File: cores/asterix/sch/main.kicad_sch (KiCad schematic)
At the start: 39 parts

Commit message: sound and pcm done! wip objects
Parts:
- added C14: 74LS138, symbol jt74:74LS138
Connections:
- net ~{RESET} renamed ~{SYSRES}
- new net ~{MCS}: C14.13 (O2)
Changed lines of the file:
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@@
+    (stroke (width 0) (type default))
+  )
+  (wire (pts (xy 118.11 250.19) (xy 125.73 250.19))
     (stroke (width 0) (type default))
   )
@@
     (effects (font (size 1.27 1.27)) (justify left))
   )
+  (hierarchical_label "~{MCS}" (shape output) (at 125.73 250.19 0) (fields_autoplaced)
+    (effects (font (size 1.27 1.27)) (justify left))
+  )
   (hierarchical_label "MAIN~{IRQ}" (shape input) (at 50.8 52.07 180) (fields_autoplaced)
     (effects (font (size 1.27 1.27)) (justify right))
@@
     (effects (font (size 1.27 1.27)) (justify left))
   )
-  (hierarchical_label "~{RESET}" (shape input) (at 48.26 80.01 180) (fields_autoplaced)
+  (hierarchical_label "~{SYSRES}" (shape input) (at 48.26 80.01 180) (fields_autoplaced)
     (effects (font (size 1.27 1.27)) (justify right))
   )
@@
         )
       )
+    )
+  )
+  (symbol (lib_id "jt74:74LS138") (at 105.41 252.73 0) (unit 1)
+    (in_bom yes) (on_board yes) (dnp no)
+    (property "Reference" "C14" (at 111.76 241.3 0)
+      (effects (font (size 1.27 1.27)))
+    )
+    (property "Value" "74LS138" (at 109.22 266.7 0)
+      (effects (font (size 1.27 1.27)))
+    )
+    (property "Footprint" "" (at 105.41 252.73 0)
+      (effects (font (size 1.27 1.27)) hide)
+    )
+    (property "Datasheet" "http://www.ti.com/lit/gpn/sn74LS138" (at 105.41 252.73 0)
+      (effects (font (size 1.27 1.27)) hide)
+    )
+    (pin "1")
+    (pin "10")
+    (pin "11")
+    (pin "12")
+    (pin "13")
+    (pin "14")
+    (pin "15")
+    (pin "2")
+    (pin "3")
+    (pin "4")
+    (pin "5")
+    (pin "6")
+    (pin "7")
+    (pin "9")
+    (instances
+      (project "asterix"
+        (path "/0011ec10-82c4-4039-b424-337480f568e8/7d4ab3ba-37fa-4111-bbdb-c99f1a708a52"
+          (reference "C14") (unit 1)
+        )
+      )

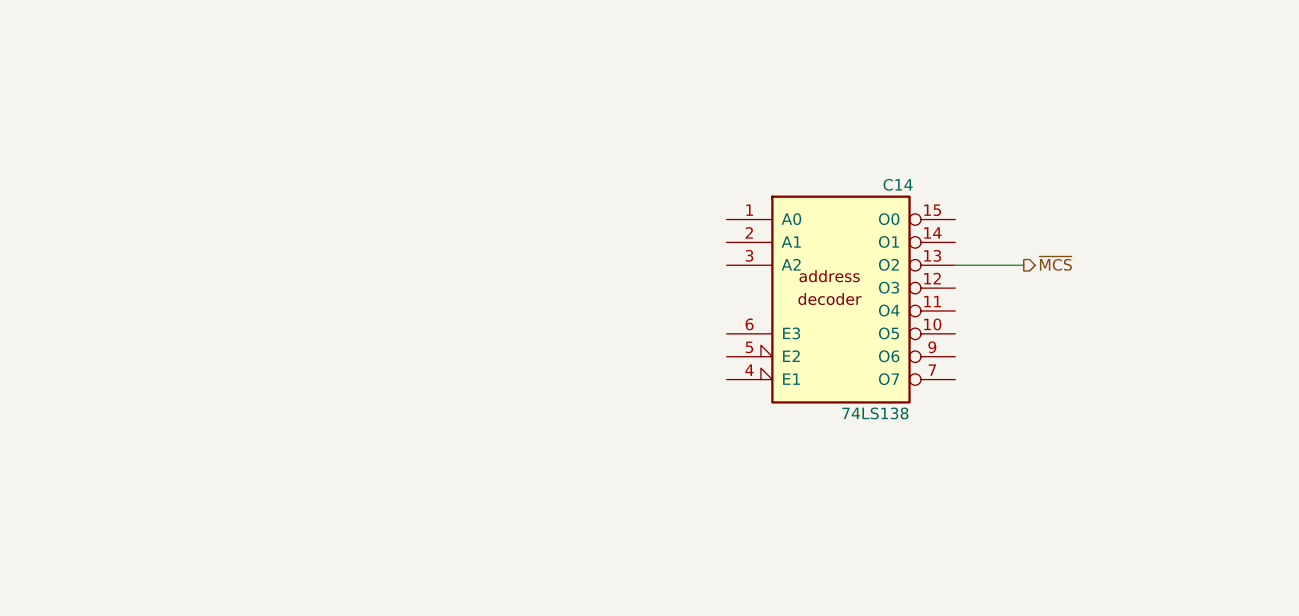
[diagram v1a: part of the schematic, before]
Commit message: objects done. wip of main, sch asterix
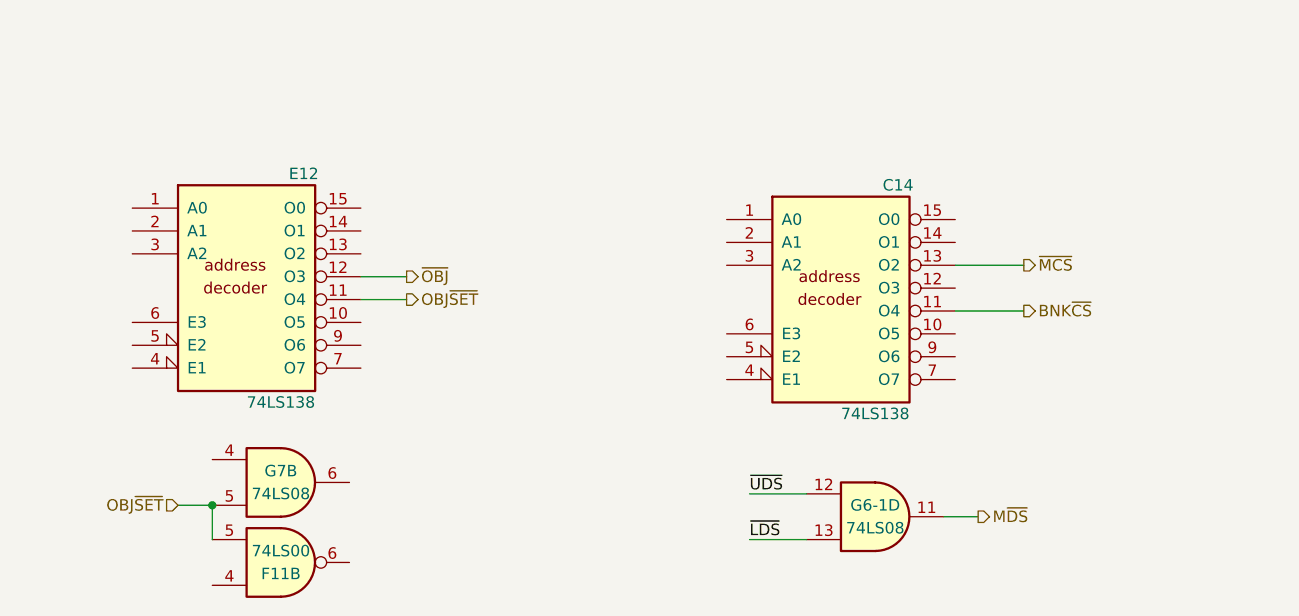
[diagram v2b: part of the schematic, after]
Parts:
- added E12: 74LS138, symbol jt74:74LS138
- added F11: 74LS00, symbol jt74:74LS00
- added G6-1, G7: 74LS08, symbol jt74:74LS08
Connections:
- net ~{LDS}: now also G6-1.13
- net ~{UDS}: now also G6-1.12
- net BNK~{CS}: now reaches C14.11 (O4)
- new net M~{DS}: G6-1.11
- new net OBJ~{SET}: E12.11 (O4), F11.5, G7.5
- new net ~{OBJ}: E12.12 (O3)
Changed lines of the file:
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@@
   (junction (at 295.91 186.69) (diameter 0) (color 0 0 0 0)
   )
+  (junction (at 35.56 276.86) (diameter 0) (color 0 0 0 0)
+  )
   (junction (at 255.27 226.06) (diameter 0) (color 0 0 0 0)
   )
@@
     (stroke (width 0) (type default))
   )
+  (wire (pts (xy 118.11 255.27) (xy 125.73 255.27))
+    (stroke (width 0) (type default))
+  )
   (bus (pts (xy 182.88 140.97) (xy 182.88 143.51))
     (stroke (width 0) (type default))
@@
     (stroke (width 0) (type default))
   )
+  (wire (pts (xy 95.25 280.67) (xy 101.6 280.67))
+    (stroke (width 0) (type default))
+  )
   (wire (pts (xy 58.42 107.95) (xy 62.23 107.95))
     (stroke (width 0) (type default))
@@
     (stroke (width 0) (type default))
   )
+  (wire (pts (xy 35.56 276.86) (xy 35.56 280.67))
+    (stroke (width 0) (type default))
+  )
   (bus (pts (xy 327.66 59.69) (xy 327.66 62.23))
     (stroke (width 0) (type default))
@@
     (stroke (width 0) (type default))
   )
+  (wire (pts (xy 52.07 254) (xy 57.15 254))
+    (stroke (width 0) (type default))
+  )
   (wire (pts (xy 69.85 34.29) (xy 86.36 34.29))
     (stroke (width 0) (type default))
@@
     (stroke (width 0) (type default))
   )
+  (wire (pts (xy 35.56 276.86) (xy 31.75 276.86))
+    (stroke (width 0) (type default))
+  )
   (wire (pts (xy 77.47 161.29) (xy 77.47 165.1))
     (stroke (width 0) (type default))
@@
     (stroke (width 0) (type default))
   )
+  (wire (pts (xy 116.84 278.13) (xy 120.65 278.13))
+    (stroke (width 0) (type default))
+  )
   (bus (pts (xy 195.58 166.37) (xy 195.58 168.91))
     (stroke (width 0) (type default))
@@
     (stroke (width 0) (type default))
   )
+  (wire (pts (xy 95.25 275.59) (xy 101.6 275.59))
+    (stroke (width 0) (type default))
+  )
   (wire (pts (xy 161.29 82.55) (xy 193.04 82.55))
     (stroke (width 0) (type default))
@@
     (stroke (width 0) (type default))
   )
+  (wire (pts (xy 52.07 251.46) (xy 57.15 251.46))
+    (stroke (width 0) (type default))
+  )
   (wire (pts (xy 274.32 186.69) (xy 267.97 186.69))
     (stroke (width 0) (type default))
@@
     (effects (font (size 1.27 1.27)) (justify left bottom))
   )
+  (label "~{LDS}" (at 95.25 280.67 0) (fields_autoplaced)
+    (effects (font (size 1.27 1.27)) (justify left bottom))
+  )
   (label "~{AS}" (at 21.59 133.35 0) (fields_autoplaced)
     (effects (font (size 1.27 1.27)) (justify left bottom))
@@
     (effects (font (size 1.27 1.27)) (justify left bottom))
   )
+  (label "~{UDS}" (at 95.25 275.59 0) (fields_autoplaced)
+    (effects (font (size 1.27 1.27)) (justify left bottom))
+  )
   (label "~{AS}" (at 170.18 151.13 180) (fields_autoplaced)
     (effects (font (size 1.27 1.27)) (justify right bottom))
@@
     (effects (font (size 1.27 1.27)) (justify left))
   )
+  (hierarchical_label "OBJ~{SET}" (shape output) (at 57.15 254 0) (fields_autoplaced)
+    (effects (font (size 1.27 1.27)) (justify left))
+  )
+  (hierarchical_label "M~{DS}" (shape output) (at 120.65 278.13 0) (fields_autoplaced)
+    (effects (font (size 1.27 1.27)) (justify left))
+  )
   (hierarchical_label "R{slash}~{W}" (shape output) (at 165.1 158.75 0) (fields_autoplaced)
     (effects (font (size 1.27 1.27)) (justify left))
   )
+  (hierarchical_label "~{OBJ}" (shape output) (at 57.15 251.46 0) (fields_autoplaced)
+    (effects (font (size 1.27 1.27)) (justify left))
+  )
   (hierarchical_label "~{UDS}" (shape output) (at 165.1 153.67 0) (fields_autoplaced)
     (effects (font (size 1.27 1.27)) (justify left))
@@
     (effects (font (size 1.27 1.27)) (justify left))
   )
+  (hierarchical_label "OBJ~{SET}" (shape input) (at 31.75 276.86 180) (fields_autoplaced)
+    (effects (font (size 1.27 1.27)) (justify right))
+  )
   (hierarchical_label "MAIN~{IRQ}" (shape input) (at 50.8 52.07 180) (fields_autoplaced)
     (effects (font (size 1.27 1.27)) (justify right))
@@
     (effects (font (size 1.27 1.27)) (justify left))
   )
+  (hierarchical_label "BNK~{CS}" (shape output) (at 125.73 255.27 0) (fields_autoplaced)
+    (effects (font (size 1.27 1.27)) (justify left))
+  )
   (hierarchical_label "~{LDS}" (shape output) (at 165.1 156.21 0) (fields_autoplaced)
     (effects (font (size 1.27 1.27)) (justify left))
@@
     (effects (font (size 1.27 1.27)) (justify right))
   )
+  (symbol (lib_id "jt74:74LS00") (at 43.18 283.21 0) (mirror x) (unit 2)
+    (in_bom yes) (on_board yes) (dnp no)
+    (property "Reference" "F11" (at 43.18 284.48 0)
+      (effects (font (size 1.27 1.27)))
+    )
+    (property "Value" "74LS00" (at 43.18 281.94 0)
+      (effects (font (size 1.27 1.27)))
+    )
+    (property "Footprint" "" (at 43.18 283.21 0)
+      (effects (font (size 1.27 1.27)) hide)
+    )
+    (property "Datasheet" "http://www.ti.com/lit/gpn/sn74ls00" (at 43.18 283.21 0)
+      (effects (font (size 1.27 1.27)) hide)
+    )
+    (pin "1")
+    (pin "2")
+    (pin "3")
+    (pin "4")
+    (pin "5")
+    (pin "6")
+    (pin "10")
+    (pin "8")
+    (pin "9")
+    (pin "11")
+    (pin "12")
+    (pin "13")
+    (pin "14")
+    (pin "7")
+    (instances
+      (project "asterix"
+        (path "/0011ec10-82c4-4039-b424-337480f568e8/f885c825-ca85-4fb9-83bd-a266030b7213"
+          (reference "F11") (unit 2)
+        )
+        (path "/0011ec10-82c4-4039-b424-337480f568e8/7d4ab3ba-37fa-4111-bbdb-c99f1a708a52"
+          (reference "F11") (unit 2)
+        )
+      )
+    )
+  )
   (symbol (lib_id "jt74:74LS32") (at 248.92 210.82 0) (mirror x) (unit 1)
     (in_bom yes) (on_board yes) (dnp no)
@@
     )
   )
+  (symbol (lib_id "jt74:74LS138") (at 39.37 251.46 0) (unit 1)
+    (in_bom yes) (on_board yes) (dnp no)
+    (property "Reference" "E12" (at 45.72 240.03 0)
+      (effects (font (size 1.27 1.27)))
+    )
+    (property "Value" "74LS138" (at 43.18 265.43 0)
+      (effects (font (size 1.27 1.27)))
+    )
+    (property "Footprint" "" (at 39.37 251.46 0)
+      (effects (font (size 1.27 1.27)) hide)
+    )
+    (property "Datasheet" "http://www.ti.com/lit/gpn/sn74LS138" (at 39.37 251.46 0)
+      (effects (font (size 1.27 1.27)) hide)
+    )
+    (pin "1")
+    (pin "10")
+    (pin "11")
+    (pin "12")
+    (pin "13")
+    (pin "14")
+    (pin "15")
+    (pin "2")
+    (pin "3")
+    (pin "4")
+    (pin "5")
+    (pin "6")
+    (pin "7")
+    (pin "9")
+    (instances
+      (project "asterix"
+        (path "/0011ec10-82c4-4039-b424-337480f568e8/7d4ab3ba-37fa-4111-bbdb-c99f1a708a52"
+          (reference "E12") (unit 1)
+        )
+      )
+    )
+  )
   (symbol (lib_id "jt74:74LS32") (at 209.55 234.95 0) (mirror x) (unit 4)
     (in_bom yes) (on_board yes) (dnp no)
@@
     )
   )
+  (symbol (lib_id "jt74:74LS08") (at 43.18 274.32 0) (unit 2)
+    (in_bom yes) (on_board yes) (dnp no)
+    (property "Reference" "G7" (at 43.18 273.05 0)
+      (effects (font (size 1.27 1.27)))
+    )
+    (property "Value" "74LS08" (at 43.18 275.59 0)
+      (effects (font (size 1.27 1.27)))
+    )
+    (property "Footprint" "" (at 43.18 274.32 0)
+      (effects (font (size 1.27 1.27)) hide)
+    )
+    (property "Datasheet" "http://www.ti.com/lit/gpn/sn74LS08" (at 43.18 274.32 0)
+      (effects (font (size 1.27 1.27)) hide)
+    )
+    (pin "1")
+    (pin "2")
+    (pin "3")
+    (pin "4")
+    (pin "5")
+    (pin "6")
+    (pin "10")
+    (pin "8")
+    (pin "9")
+    (pin "11")
+    (pin "12")
+    (pin "13")
+    (pin "14")
+    (pin "7")
+    (instances
+      (project "asterix"
+        (path "/0011ec10-82c4-4039-b424-337480f568e8/f885c825-ca85-4fb9-83bd-a266030b7213"
+          (reference "G7") (unit 2)
+        )
+        (path "/0011ec10-82c4-4039-b424-337480f568e8/7d4ab3ba-37fa-4111-bbdb-c99f1a708a52"
+          (reference "G7") (unit 2)
+        )
+      )
+      (project "sriders"
+        (path "/df39d662-4aa2-4ddc-b42d-33d6757a8623/78ffae6e-b754-4ff0-aaab-f5e038ba4a01"
+          (reference "G15") (unit 1)
+        )
+      )
+    )
+  )
   (symbol (lib_id "jt74:74LS74") (at 62.23 36.83 0) (unit 2)
     (in_bom yes) (on_board yes) (dnp no)
@@
         )
       )
+    )
+  )
+  (symbol (lib_id "jt74:74LS08") (at 109.22 278.13 0) (unit 4)
+    (in_bom yes) (on_board yes) (dnp no)
+    (property "Reference" "G6-1" (at 109.22 276.86 0)
+      (effects (font (size 1.27 1.27)))
+    )
+    (property "Value" "74LS08" (at 109.22 279.4 0)
+      (effects (font (size 1.27 1.27)))
+    )
+    (property "Footprint" "" (at 109.22 278.13 0)
+      (effects (font (size 1.27 1.27)) hide)
+    )
+    (property "Datasheet" "http://www.ti.com/lit/gpn/sn74LS08" (at 109.22 278.13 0)
+      (effects (font (size 1.27 1.27)) hide)
+    )
+    (pin "1")
+    (pin "2")
+    (pin "3")
+    (pin "4")
+    (pin "5")
+    (pin "6")
+    (pin "10")
+    (pin "8")
+    (pin "9")
+    (pin "11")
+    (pin "12")
+    (pin "13")
+    (pin "14")
+    (pin "7")
+    (instances
+      (project "asterix"
+        (path "/0011ec10-82c4-4039-b424-337480f568e8/fce18e79-2cc3-4aa0-a9fd-760414886979"
+          (reference "G6-1") (unit 4)
+        )
+        (path "/0011ec10-82c4-4039-b424-337480f568e8/f885c825-ca85-4fb9-83bd-a266030b7213"
+          (reference "G6-1") (unit 2)
+        )
+        (path "/0011ec10-82c4-4039-b424-337480f568e8/7d4ab3ba-37fa-4111-bbdb-c99f1a708a52"
+          (reference "G6-1") (unit 2)
+        )
+      )

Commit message: wip main sch asterix
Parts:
- removed B?, C? (x4), F? (x8): 74LS32, symbol jt74:74LS32
- removed C?: GAL22V10, symbol Logic_Programmable:PAL20RS10
- removed CP? (x2): 104, symbol Device:C_Small
- removed D? (x2), F? (x2): 27C020, symbol Memory_EPROM:27C020
- removed E? (x4), H?: 74LS04, symbol jt74:74LS04
- removed E? (x3): 74LS00, symbol jt74:74LS00
- removed E?: 74LS74, symbol jt74:74LS74
- removed F?: 74LS08, symbol jt74:74LS08
- added B13: 74LS20, symbol jt74:74LS20
- added C13: 74LS139, symbol jt74:74LS139
- added C7, C8, D7, D8: 27C010, symbol Memory_EPROM:27C010
- added CP41, CP42: 104, symbol Device:C_Small
- added D18 (x2): 74LS32, symbol jt74:74LS32
- added F11 (x2): 74LS00, symbol jt74:74LS00
- added G3: XTAL_OSC, symbol Device:Crystal_GND23_Small
- added G4 (x2): 74LS04, symbol jt74:74LS04
- gave numbers to parts that had none: 8
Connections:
- net MCLK is gone; now on an unnamed net: D10.15 (CLK)
- net GND: now also C7.16 (GND), C8.16 (GND), CP41.2, CP42.2, D7.16 (GND), D8.16 (GND)
- net MAIN_A1: now also C7.12 (A0), C8.12 (A0), D7.12 (A0), D8.12 (A0)
- net MAIN_A10: now also C14.3 (A2), C7.26 (A9), C8.26 (A9), D7.26 (A9), D8.26 (A9)
- net MAIN_A11: now also C7.23 (A10), C8.23 (A10), D7.23 (A10), D8.23 (A10)
- net MAIN_A12: now also C7.25 (A11), C8.25 (A11), D7.25 (A11), D8.25 (A11)
- net MAIN_A13: now also C7.4 (A12), C8.4 (A12), D7.4 (A12), D8.4 (A12)
- net MAIN_A14: now also F7.26 (CS2), F8.26 (CS2), C7.28 (A13), C8.28 (A13), D7.28 (A13), D8.28 (A13)
- net MAIN_A15: now also F7.1 (NC), F8.1 (NC), C7.29 (A14), C8.29 (A14), D7.29 (A14), D8.29 (A14)
- net MAIN_A16: now also C7.3 (A15), C8.3 (A15), D7.3 (A15), D8.3 (A15)
- net MAIN_A17: now also C7.2 (A16), C8.2 (A16), D7.2 (A16), D8.2 (A16)
- net MAIN_A19: now also E12.1 (A0)
- net MAIN_A2: now also C7.11 (A1), C8.11 (A1), D7.11 (A1), D8.11 (A1)
- net MAIN_A20: now also E12.2 (A1)
- net MAIN_A22: now also E12.3 (A2)
- net MAIN_A3: now also C7.10 (A2), C8.10 (A2), D7.10 (A2), D8.10 (A2)
- net MAIN_A4: now also C7.9 (A3), C8.9 (A3), D7.9 (A3), D8.9 (A3)
- net MAIN_A5: now also C7.8 (A4), C8.8 (A4), D7.8 (A4), D8.8 (A4)
- net MAIN_A6: now also C7.7 (A5), C8.7 (A5), D7.7 (A5), D8.7 (A5)
- net MAIN_A7: now also C7.6 (A6), C8.6 (A6), D7.6 (A6), D8.6 (A6)
- net MAIN_A8: now also C14.1 (A0), C7.5 (A7), C8.5 (A7), D7.5 (A7), D8.5 (A7)
- net MAIN_A9: now also C14.2 (A1), C7.27 (A8), C8.27 (A8), D7.27 (A8), D8.27 (A8)
- net MAIN_D0: now also D7.13 (D0), D8.13 (D0)
- net MAIN_D1: now also D7.14 (D1), D8.14 (D1)
- net MAIN_D10: now also C7.15 (D2), C8.15 (D2)
- net MAIN_D11: now also C7.17 (D3), C8.17 (D3)
- net MAIN_D12: now also C7.18 (D4), C8.18 (D4)
- net MAIN_D13: now also C7.19 (D5), C8.19 (D5)
- net MAIN_D14: now also C7.20 (D6), C8.20 (D6)
- net MAIN_D15: now also C7.21 (D7), C8.21 (D7)
- net MAIN_D2: now also D7.15 (D2), D8.15 (D2)
- net MAIN_D3: now also D7.17 (D3), D8.17 (D3)
- net MAIN_D4: now also D7.18 (D4), D8.18 (D4)
- net MAIN_D5: now also D7.19 (D5), D8.19 (D5)
- net MAIN_D6: now also D7.20 (D6), D8.20 (D6)
- net MAIN_D7: now also D7.21 (D7), D8.21 (D7)
- net MAIN_D8: now also C7.13 (D0), C8.13 (D0)
- net MAIN_D9: now also C7.14 (D1), C8.14 (D1)
- net M~{RD}: now also C7.22 (~{CE}), C8.22 (~{CE}), D7.22 (~{CE}), D8.22 (~{CE}), G4.10
- net PAS: now also B13.9, G4.10
- net R/~{W}: now also G4.11
- net VCC: now also D10.24 (IPL1), C13.16 (VCC), C7.1 (VPP), C7.31 (~{PGM}), C7.32 (VCC), C8.1 (VPP), C8.31 (~{PGM}), C8.32 (VCC), CP41.1, CP42.1, D7.1 (VPP), D7.31 (~{PGM}), D7.32 (VCC), D8.1 (VPP), D8.31 (~{PGM}), D8.32 (VCC), G3.4; no longer D10.12 (BGACK), D10.13 (BR), D10.22 (BERR), F7.26 (CS2), F8.26 (CS2)
- net VSS: now also C13.8 (VSS), G3.1, G3.2; no longer B11.12 (D), F7.20 (~{CS1}), F8.20 (~{CS1})
- net ~{AS}: now also G4.11
- net ~{SYSRES}: now also B18-1.11; no longer B18-1.5
- net at B11.11 (C): now also G3.3
- net at C14.4 (E1): now also C13.13 (A1)
- net at B18-1.4, RA10.3 (R2): now also D10.17 (HALT); no longer D10.18 (RESET)
- net RAM~{OE}: now reaches F7.22 (~{OE}), F8.22 (~{OE})
- net RAM~{OE}: now also E12.10 (O5), D18.5, D18.5
- net ~{CS1}: now reaches E12.13 (O2)
- net ~{CS1}: now also F7.20 (~{CS1}), F8.20 (~{CS1})
- net ~{OE}2: now reaches E12.14 (O1)
- net ~{OE}2: now also C7.24 (~{OE}), D7.24 (~{OE})
- net ~{OE}1: now reaches E12.15 (O0)
- net ~{OE}1: now also C8.24 (~{OE}), D8.24 (~{OE})
- net at B11.8 (~{Q}): now also B11.12 (D)
- net ~{IPL0}: now reaches D10.25 (IPL0)
- net DTACK: now reaches D10.10 (DTACK)
- net ~{BG}: now reaches D10.11 (BG)
- net at D10.21 (VPA): now also B13.8
- net at D10.26 (FC2): now also B13.13
- net at D10.27 (FC1): now also B13.12
- net at D10.28 (FC0): now also B13.10
- net INTDMA: no longer names the net of B11.9 (Q)
- net INTDMAEN: no longer names the net of B11.10 (~{S})
- net MRAM~{WE}H renamed ~{WE}H
- net ~{WE}H: now also D18.4, F11.6
- net MRAM~{WE}L renamed ~{WE}L
- net ~{WE}L: now also D18.4, F11.6
- new net: B18-1.10, D10.18 (RESET), RA10.2 (R1)
- new net ~{BGACK}: D10.12 (BGACK)
- new net ~{BR}: D10.13 (BR)
- no-connect marks 11 -> 4
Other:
- note added: "24.00000MHz"
- note added: "CMOS EPROM 1M-BIT [128K x 8]"
- note added: "KONAMI 054860"
- note added: "LH5168D-10L"
- note added: "MC68000P12"
- note added: "PIN52 054156"
- note removed: "16MHz"
- note removed: "MASK 2M"
- note removed: "THERE ARE NO EQUATIONS STORED IN JEDUTIL, FROM THE GAL22V10 DEVICE (Konami_054683)"
- note removed: "VSS"
- moved on the sheet: B11B, B18-1B, B18-1E, C14, E12, F11B, G6-1D, G7B, RA10

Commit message: main done. wip colmix asterix
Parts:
- removed unit 3 of C13
- removed F11: 74LS00, symbol jt74:74LS00
- added D13, F10: 74LS04, symbol jt74:74LS04
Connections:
- net MAIN_A11: now also C14.4 (E1)
- net MAIN_A17: now also C13.2 (A0)
- net MAIN_A18: now also C13.3 (A1)
- net MAIN_A22: now also C13.14 (A0), D13.11
- net MAIN_A23: now also C13.13 (A1), E12.4 (E1)
- net M~{DS}: now also D13.1
- net M~{RD}: now also F11.5
- net OBJ~{SET}: now also E12.9 (O6); no longer E12.11 (O4), G7.5
- net R/~{W}: now also RA10.6 (R5); no longer RA10.4 (R3)
- net ~{AS}: now also C13.15 (E), E12.5 (E2)
- net ~{OBJ}: now also F11.4
- net ~{SYSRES}: now also G7.4
- net ~{UDS}: now also RA10.4 (R3), F10.3; no longer RA10.6 (R5)
- net at F11.5: now also E12.11 (O4), G7.5
- net ~{E2}: now reaches C14.5 (E2)
- net ~{E2}: now also E12.7 (O7)
- net at C14.6 (E3): now also D13.2
- net PIN21 18E: now reaches D18.6
- net at C13.1 (E): now also C13.11 (O1)
- net at E12.6 (E3): now also D13.10
- net MOBJ~{RD}: now reaches G7.6
- net at F11.4: now also F10.4
- net PIN21 19E: now reaches D18.6
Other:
- moved on the sheet: B11B, B13B, B18-1B, B18-1E, C13A, C13B, C14, C7, C8, CC2, CC3, CP41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

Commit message: uk konami 054358 done. wip colmix
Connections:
- net ~{E2} renamed ~{IO}
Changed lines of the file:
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@@
     (stroke (width 0) (type default))
   )
-  (wire (pts (xy 218.44 220.98) (xy 228.6 220.98))
+  (wire (pts (xy 218.44 220.98) (xy 223.52 220.98))
     (stroke (width 0) (type default))
   )
@@
     (effects (font (size 1.27 1.27)) (justify left bottom))
   )
-  (label "~{E2}" (at 180.34 266.7 0) (fields_autoplaced)
+  (label "~{IO}" (at 180.34 266.7 0) (fields_autoplaced)
     (effects (font (size 1.27 1.27)) (justify left bottom))
   )
@@
   (label "MAIN_A23" (at 180.34 220.98 0) (fields_autoplaced)
     (effects (font (size 1.27 1.27)) (justify left bottom))
-  )
-  (label "~{E2}" (at 228.6 220.98 180) (fields_autoplaced)
-    (effects (font (size 1.27 1.27)) (justify right bottom))
   )
   (label "MAIN_A14" (at 248.92 153.67 0) (fields_autoplaced)
@@
     (effects (font (size 1.27 1.27)) (justify left))
   )
+  (hierarchical_label "~{IO}" (shape output) (at 223.52 220.98 0) (fields_autoplaced)
+    (effects (font (size 1.27 1.27)) (justify left))
+  )
